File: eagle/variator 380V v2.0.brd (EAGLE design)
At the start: 65 x 94.3 mm, 31 parts, among them P1 BANANA, P2 BANANA, P3 BANANA, P4 BANANA

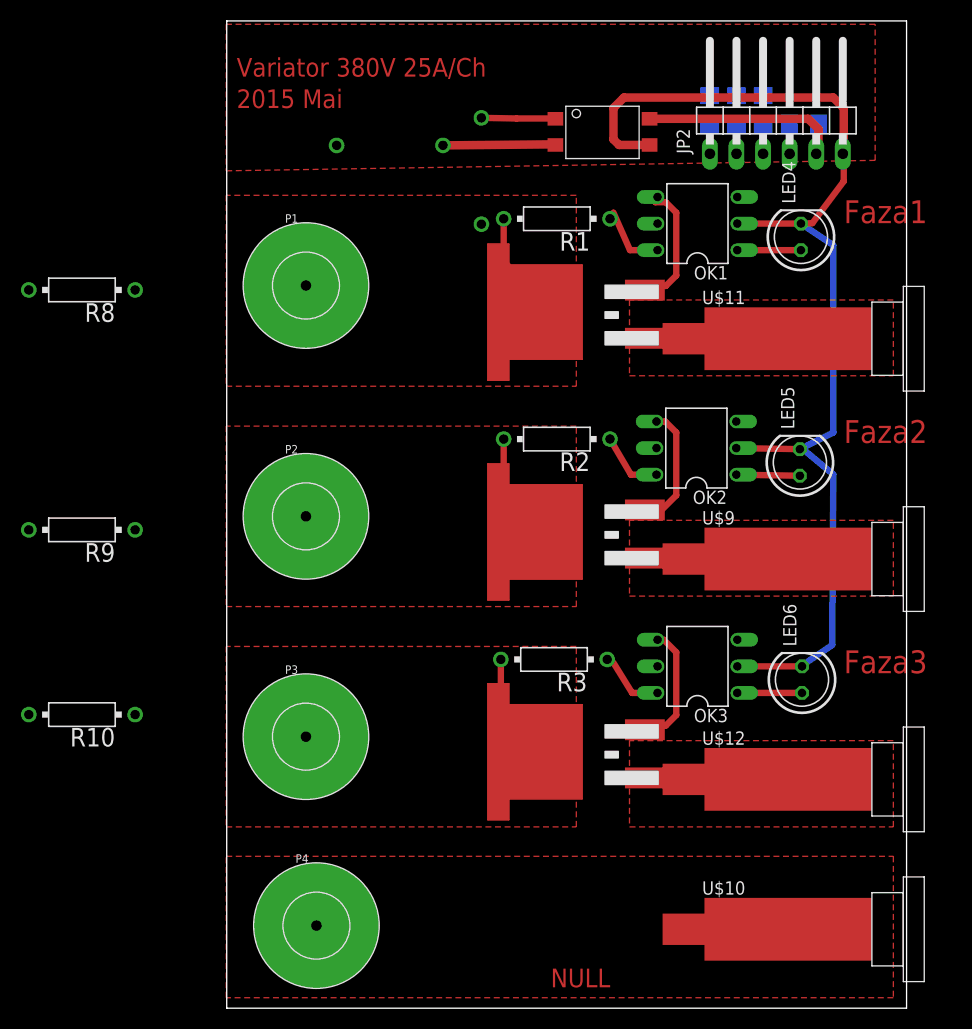
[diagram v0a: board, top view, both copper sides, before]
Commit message: Resistenta separate la fiecare led in parte. Led in parallel connection.
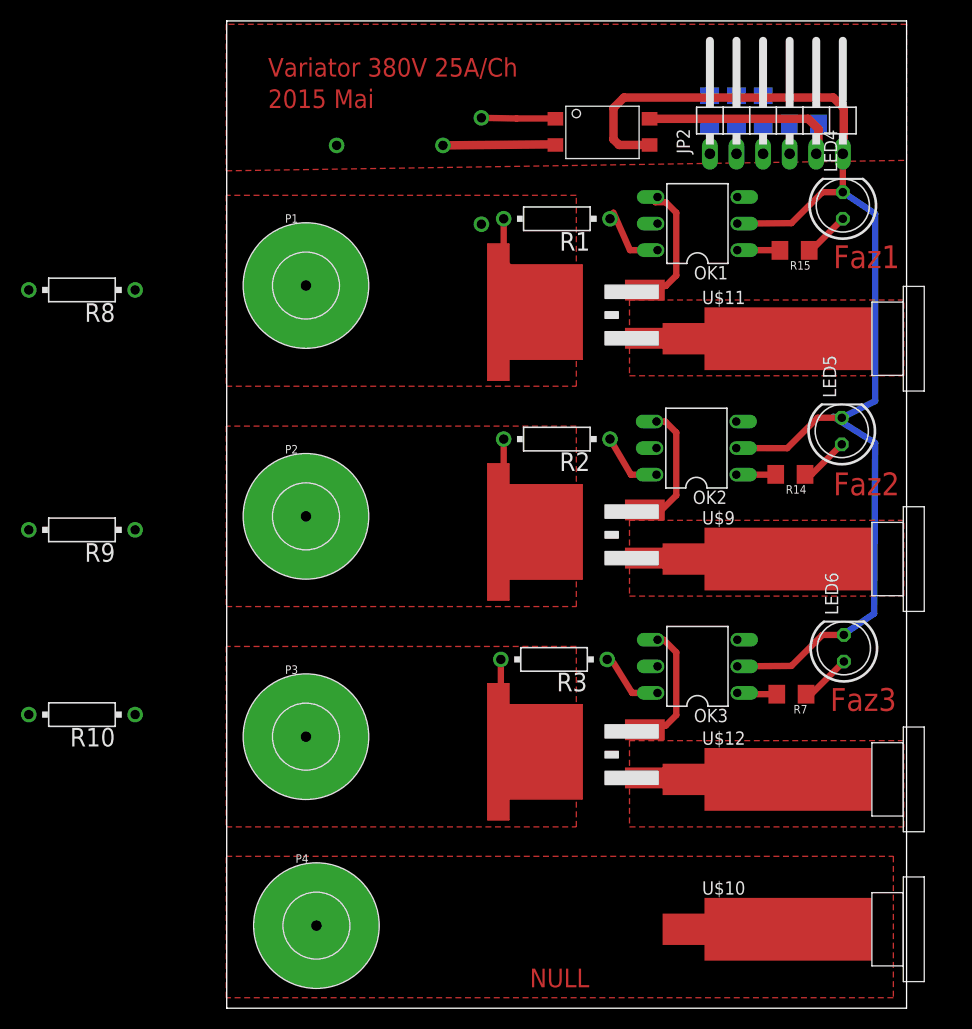
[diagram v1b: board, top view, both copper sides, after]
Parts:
- added R14, R15, R7: 76, adi_v1.4:1206
- R5, R6: value 110 -> 44.1
- moved LED4 5.00 mm to (58.9, 76.7)
- moved LED5 5.00 mm to (58.8, 55.1)
- moved LED6 5.00 mm to (59.0, 34.4)
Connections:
- new net N$12: OK1.1, R15.2
- new net N$8: OK3.1, R7.2
- new net N$9: OK2.1, R14.2
- net N$10: now also R14.1; no longer OK2.1
- net N$11: now also R7.1; no longer OK3.1
- net N$7: now also R15.1; no longer OK1.1
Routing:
- net GND: track 111.9 -> 123.9 mm
- net N$12: track 0.00 -> 4.09 mm
- net N$8: track 0.00 -> 3.89 mm
- net N$9: track 0.00 -> 3.80 mm
- net N$7: track 6.08 -> 4.46 mm
- net N$10: track 6.08 -> 4.70 mm
- net N$11: track 6.18 -> 4.90 mm
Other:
- board text added: "Faz1"
- board text added: "Faz2"
- board text added: "Faz3"
- board text removed: "Faza1"
- board text removed: "Faza2"
- board text removed: "Faza3"
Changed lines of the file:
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@@
 <wire x1="65" y1="94.32" x2="0.05" y2="94.32" width="0" layer="20"/>
 <wire x1="0.05" y1="94.32" x2="0.05" y2="0" width="0" layer="20"/>
-<text x="31" y="2" size="1.778" layer="1" font="vector">NULL</text>
-<text x="59" y="75" size="2.1844" layer="1">Faza1</text>
-<text x="59" y="54" size="2.1844" layer="1">Faza2</text>
-<text x="59" y="32" size="2.1844" layer="1">Faza3</text>
-<text x="1" y="89" size="1.778" layer="1" font="vector">Variator 380V 25A/Ch</text>
-<text x="1" y="86" size="1.778" layer="1" font="vector">2015 Mai</text>
+<text x="29" y="2" size="1.778" layer="1" font="vector">NULL</text>
+<text x="58" y="70.7" size="2.1844" layer="1">Faz1</text>
+<text x="58" y="49" size="2.1844" layer="1">Faz2</text>
+<text x="57.7" y="28.4" size="2.1844" layer="1">Faz3</text>
+<text x="4" y="89" size="1.778" layer="1" font="vector">Variator 380V 25A/Ch</text>
+<text x="4" y="86" size="1.778" layer="1" font="vector">2015 Mai</text>
 </plain>
 <attributes>
@@
 <elements>
 <element name="JP2" library="pinhead" package="1X06/90" value="" x="52.56" y="85.44"/>
-<element name="LED4" library="led" package="LED5MM" value="" x="54.91" y="73.69" rot="R90"/>
-<element name="LED5" library="led" package="LED5MM" value="" x="54.81" y="52.14" rot="R90"/>
-<element name="LED6" library="led" package="LED5MM" value="" x="55.01" y="31.39" rot="R90"/>
+<element name="LED4" library="led" package="LED5MM" value="" x="58.91" y="76.69" rot="R90"/>
+<element name="LED5" library="led" package="LED5MM" value="" x="58.81" y="55.14" rot="R90"/>
+<element name="LED6" library="led" package="LED5MM" value="" x="59.01" y="34.39" rot="R90"/>
 <element name="OK1" library="optocoupler" package="DIL06" value="IL410" x="45.02" y="74.96" rot="R90">
 <attribute name="OC_NEWARK" value="58K1715" x="45.02" y="74.96" size="1.778" layer="27" rot="R90" display="off"/>
@@
 </element>
 <element name="R4" library="adi_v1.4" package="1206" value="110" x="51.31" y="85.78" rot="MR90"/>
-<element name="R5" library="adi_v1.4" package="1206" value="110" x="48.75" y="85.78" rot="MR90"/>
-<element name="R6" library="adi_v1.4" package="1206" value="110" x="46.19" y="85.78" rot="MR90"/>
+<element name="R5" library="adi_v1.4" package="1206" value="44.1" x="48.75" y="85.78" rot="MR90"/>
+<element name="R6" library="adi_v1.4" package="1206" value="44.1" x="46.19" y="85.78" rot="MR90"/>
 <element name="R8" library="resistor-power" package="HPS58" value="500k" x="-13.78" y="68.62" rot="R180">
 <attribute name="OC_NEWARK" value="unknown" x="-13.78" y="68.62" size="1.778" layer="27" rot="R180" display="off"/>
@@
 <element name="U$2" library="Serghei IR station" package="TO-263" value="Q8025NH6RP" x="40" y="43" rot="R90"/>
 <element name="U$3" library="Serghei IR station" package="TO-263" value="Q8025NH6RP" x="40" y="22" rot="R90"/>
+<element name="R7" library="adi_v1.4" package="1206" value="76" x="54" y="30" rot="R180"/>
+<element name="R14" library="adi_v1.4" package="1206" value="76" x="53.9" y="51" rot="R180"/>
+<element name="R15" library="adi_v1.4" package="1206" value="76" x="54.3" y="72.4" rot="R180"/>
 </elements>
 <signals>
@@
 <vertex x="38.53" y="67.66"/>
 <vertex x="38.53" y="60.42"/>
-<vertex x="63.74" y="60.42"/>
-<vertex x="63.74" y="67.66"/>
+<vertex x="64.74" y="60.42"/>
+<vertex x="64.74" y="67.66"/>
 </polygon>
 <contactref element="U$1" pad="T1"/>
@@
 <polygon width="0.4064" layer="1" isolate="2.54" thermals="no">
 <vertex x="38.53" y="39.37"/>
-<vertex x="63.74" y="39.37"/>
-<vertex x="63.74" y="46.61"/>
+<vertex x="64.74" y="39.37"/>
+<vertex x="64.74" y="46.61"/>
 <vertex x="38.53" y="46.61"/>
 </polygon>
@@
 <vertex x="38.53" y="25.56"/>
 <vertex x="38.53" y="17.32"/>
-<vertex x="63.74" y="17.32"/>
-<vertex x="63.74" y="25.56"/>
+<vertex x="64.74" y="17.32"/>
+<vertex x="64.74" y="25.56"/>
 </polygon>
 <contactref element="U$3" pad="T1"/>
@@
 </signal>
 <signal name="N$7">
-<contactref element="OK1" pad="1"/>
 <contactref element="R4" pad="2"/>
 <contactref element="LED4" pad="A"/>
-<wire x1="54.91" y1="72.42" x2="48.83" y2="72.42" width="0.6096" layer="1"/>
-<wire x1="48.83" y1="72.42" x2="51.31" y2="87.18" width="0" layer="19" extent="16-16"/>
+<contactref element="R15" pad="1"/>
+<wire x1="55.7" y1="72.4" x2="55.89" y2="72.4" width="0.6096" layer="1"/>
+<wire x1="55.89" y1="72.4" x2="58.91" y2="75.42" width="0.6096" layer="1"/>
+<wire x1="58.91" y1="75.42" x2="51.31" y2="87.18" width="0" layer="19" extent="16-16"/>
 </signal>
 <signal name="N$10">
-<contactref element="OK2" pad="1"/>
 <contactref element="R5" pad="2"/>
 <contactref element="LED5" pad="A"/>
-<wire x1="54.81" y1="50.87" x2="48.73" y2="50.97" width="0.6096" layer="1"/>
-<wire x1="48.73" y1="50.97" x2="48.75" y2="87.18" width="0" layer="19" extent="16-16"/>
+<contactref element="R14" pad="1"/>
+<wire x1="55.3" y1="51" x2="55.94" y2="51" width="0.6096" layer="1"/>
+<wire x1="55.94" y1="51" x2="58.81" y2="53.87" width="0.6096" layer="1"/>
+<wire x1="58.81" y1="53.87" x2="48.75" y2="87.18" width="0" layer="19" extent="16-16"/>
 </signal>
 <signal name="N$11">
-<contactref element="OK3" pad="1"/>
 <contactref element="R6" pad="2"/>
 <contactref element="LED6" pad="A"/>
-<wire x1="55.01" y1="30.12" x2="48.83" y2="30.12" width="0.6096" layer="1"/>
-<wire x1="48.83" y1="30.12" x2="46.19" y2="87.18" width="0" layer="19" extent="16-16"/>
+<contactref element="R7" pad="1"/>
+<wire x1="55.4" y1="30" x2="55.89" y2="30" width="0.6096" layer="1"/>
+<wire x1="55.89" y1="30" x2="59.01" y2="33.12" width="0.6096" layer="1"/>
+<wire x1="59.01" y1="33.12" x2="46.19" y2="87.18" width="0" layer="19" extent="16-16"/>
 </signal>
 <signal name="N$14">
@@
 <contactref element="OK3" pad="2"/>
 <contactref element="LED6" pad="K"/>
-<wire x1="55.01" y1="32.66" x2="48.83" y2="32.66" width="0.6096" layer="1"/>
-<wire x1="54.91" y1="74.96" x2="48.83" y2="74.96" width="0.6096" layer="1"/>
+<wire x1="59.01" y1="35.66" x2="56.96" y2="35.66" width="0.6096" layer="1"/>
+<wire x1="56.96" y1="35.66" x2="54" y2="32.7" width="0.6096" layer="1"/>
+<wire x1="54" y1="32.7" x2="48.83" y2="32.66" width="0.6096" layer="1"/>
+<wire x1="58.91" y1="77.96" x2="56.96" y2="77.96" width="0.6096" layer="1"/>
+<wire x1="56.96" y1="77.96" x2="54" y2="75" width="0.6096" layer="1"/>
+<wire x1="54" y1="75" x2="48.83" y2="74.96" width="0.6096" layer="1"/>
 <wire x1="58.91" y1="80.36" x2="58.91" y2="81.63" width="0.4064" layer="1"/>
 <wire x1="40.45" y1="82.47" x2="37.53" y2="82.47" width="0.8128" layer="1"/>
@@
 <wire x1="59" y1="86" x2="59" y2="81.72" width="0.8128" layer="1"/>
 <wire x1="59" y1="81.72" x2="58.91" y2="81.63" width="0.8128" layer="1"/>
-<wire x1="55.01" y1="32.66" x2="54.76" y2="32.56" width="0.4064" layer="16"/>
-<wire x1="54.76" y1="32.56" x2="57.9" y2="34.7" width="0.6096" layer="16"/>
-<wire x1="57.9" y1="34.7" x2="58" y2="51" width="0.6096" layer="16"/>
-<wire x1="58" y1="51" x2="55" y2="53.5" width="0.6096" layer="16"/>
-<wire x1="54.81" y1="53.41" x2="55" y2="53.5" width="0.6096" layer="16"/>
-<wire x1="54.81" y1="53.41" x2="58" y2="55" width="0.6096" layer="16"/>
-<wire x1="58" y1="55" x2="58" y2="72.9" width="0.6096" layer="16"/>
-<wire x1="58" y1="72.9" x2="54.91" y2="74.96" width="0.6096" layer="16"/>
-<wire x1="54.91" y1="74.96" x2="54.96" y2="74.96" width="0.6096" layer="1"/>
-<wire x1="54.96" y1="74.96" x2="56" y2="75" width="0.6096" layer="1"/>
-<wire x1="56" y1="75" x2="59" y2="79" width="0.6096" layer="1"/>
-<wire x1="59" y1="79" x2="59" y2="81.54" width="0.6096" layer="1"/>
-<wire x1="59" y1="81.54" x2="58.91" y2="81.63" width="0.4064" layer="1"/>
-<wire x1="54.81" y1="53.41" x2="48.73" y2="53.51" width="0.6096" layer="1"/>
+<wire x1="59.01" y1="35.66" x2="58.76" y2="35.56" width="0.4064" layer="16"/>
+<wire x1="58.76" y1="35.56" x2="61.9" y2="37.7" width="0.6096" layer="16"/>
+<wire x1="61.9" y1="37.7" x2="62" y2="54" width="0.6096" layer="16"/>
+<wire x1="62" y1="54" x2="58" y2="56.5" width="0.6096" layer="16"/>
+<wire x1="58.81" y1="56.41" x2="58" y2="56.5" width="0.6096" layer="16"/>
+<wire x1="58.81" y1="56.41" x2="62" y2="58" width="0.6096" layer="16"/>
+<wire x1="62" y1="58" x2="62" y2="75.9" width="0.6096" layer="16"/>
+<wire x1="62" y1="75.9" x2="58.91" y2="77.96" width="0.6096" layer="16"/>
+<wire x1="58.81" y1="56.41" x2="56.51" y2="56.41" width="0.6096" layer="1"/>
+<wire x1="56.51" y1="56.41" x2="53.6" y2="53.5" width="0.6096" layer="1"/>
+<wire x1="53.6" y1="53.5" x2="48.73" y2="53.51" width="0.6096" layer="1"/>
+<wire x1="58.91" y1="77.96" x2="58.91" y2="81.63" width="0.6096" layer="1"/>
 </signal>
 <signal name="NONE">
-<polygon width="0.8128" layer="1" isolate="1.4224">
+<polygon width="0.8128" layer="1" isolate="0.8128">
 <vertex x="0" y="94"/>
 <vertex x="0" y="80"/>
-<vertex x="62" y="81"/>
-<vertex x="62" y="94"/>
-</polygon>
+<vertex x="65" y="81"/>
+<vertex x="65" y="94"/>
+</polygon>
+</signal>
+<signal name="N$8">
+<contactref element="OK3" pad="1"/>
+<contactref element="R7" pad="2"/>
+<wire x1="52.6" y1="30" x2="48.83" y2="30" width="0.6096" layer="1"/>
+<wire x1="48.83" y1="30" x2="48.83" y2="30.12" width="0.6096" layer="1"/>
+</signal>
+<signal name="N$9">
+<contactref element="OK2" pad="1"/>
+<contactref element="R14" pad="2"/>
+<wire x1="48.73" y1="50.97" x2="52.5" y2="50.97" width="0.6096" layer="1"/>
+<wire x1="52.5" y1="50.97" x2="52.5" y2="51" width="0.6096" layer="1"/>
+</signal>
+<signal name="N$12">
+<contactref element="OK1" pad="1"/>
+<contactref element="R15" pad="2"/>
+<wire x1="48.83" y1="72.42" x2="52.9" y2="72.42" width="0.6096" layer="1"/>
+<wire x1="52.9" y1="72.42" x2="52.9" y2="72.4" width="0.6096" layer="1"/>
 </signal>
 </signals>
